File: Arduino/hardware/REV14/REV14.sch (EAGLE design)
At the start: 27 parts, among them IC2 ATMEGA168-AU, Q1 32768Hz, U1 RN2483, U2 TMP112, X1 SMA-142-0701-881/886, X2 SMA-142-0701-881/886

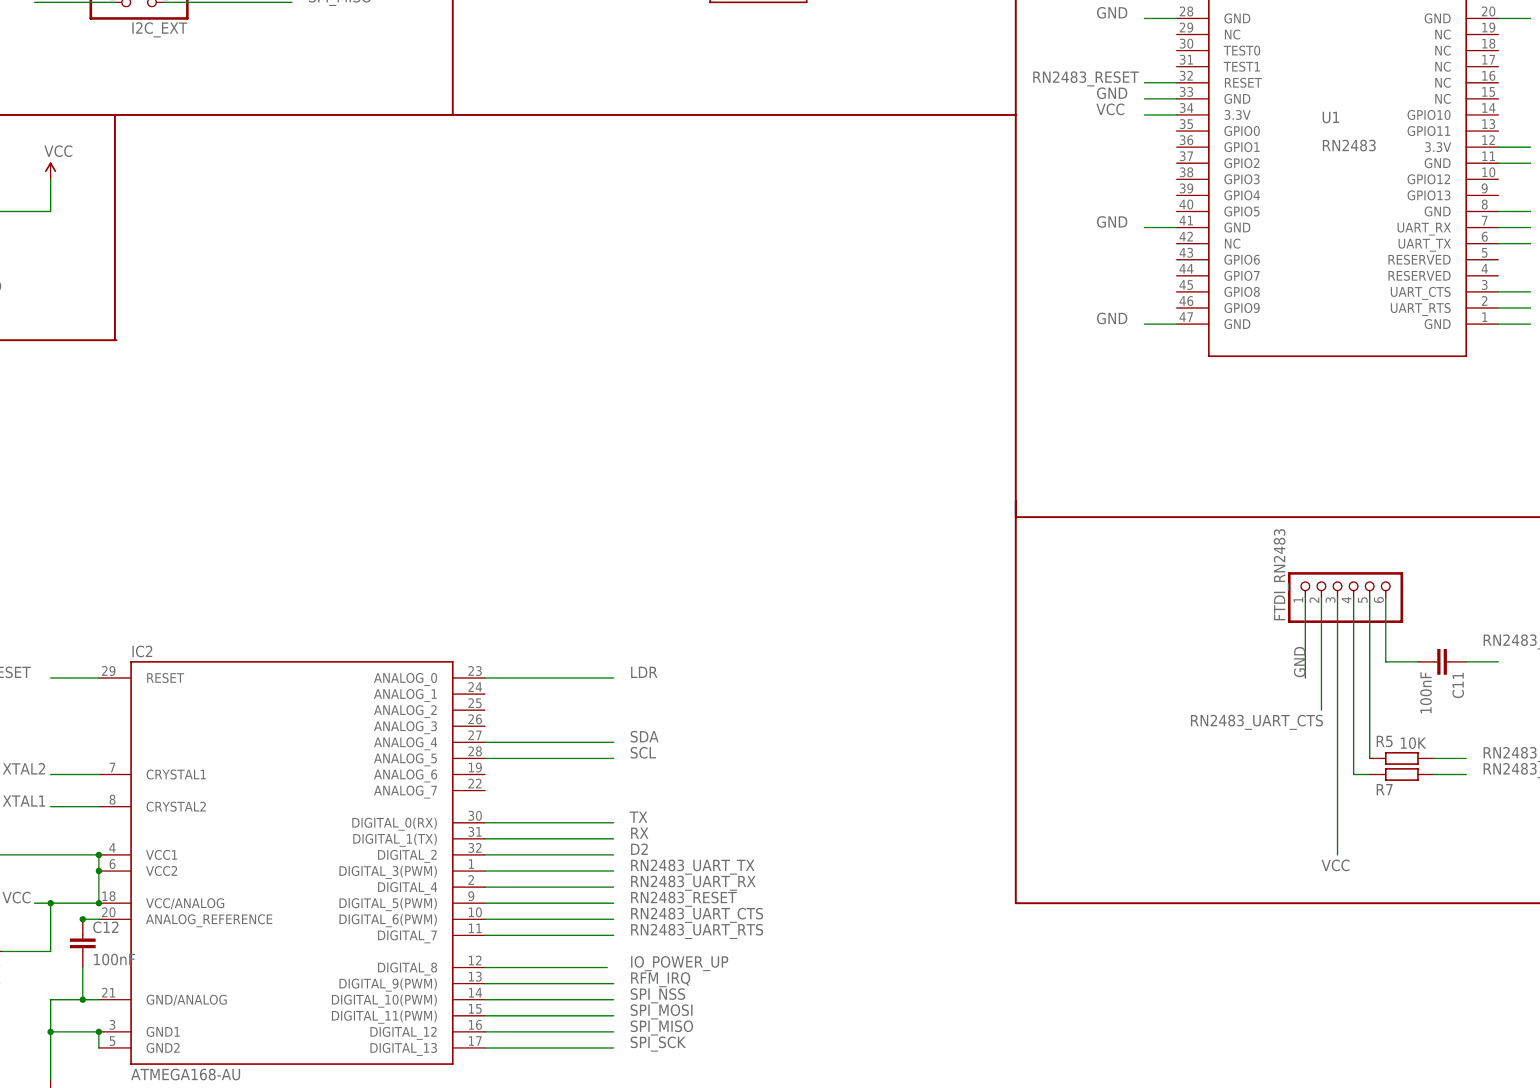
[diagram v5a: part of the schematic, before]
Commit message: charge pump added
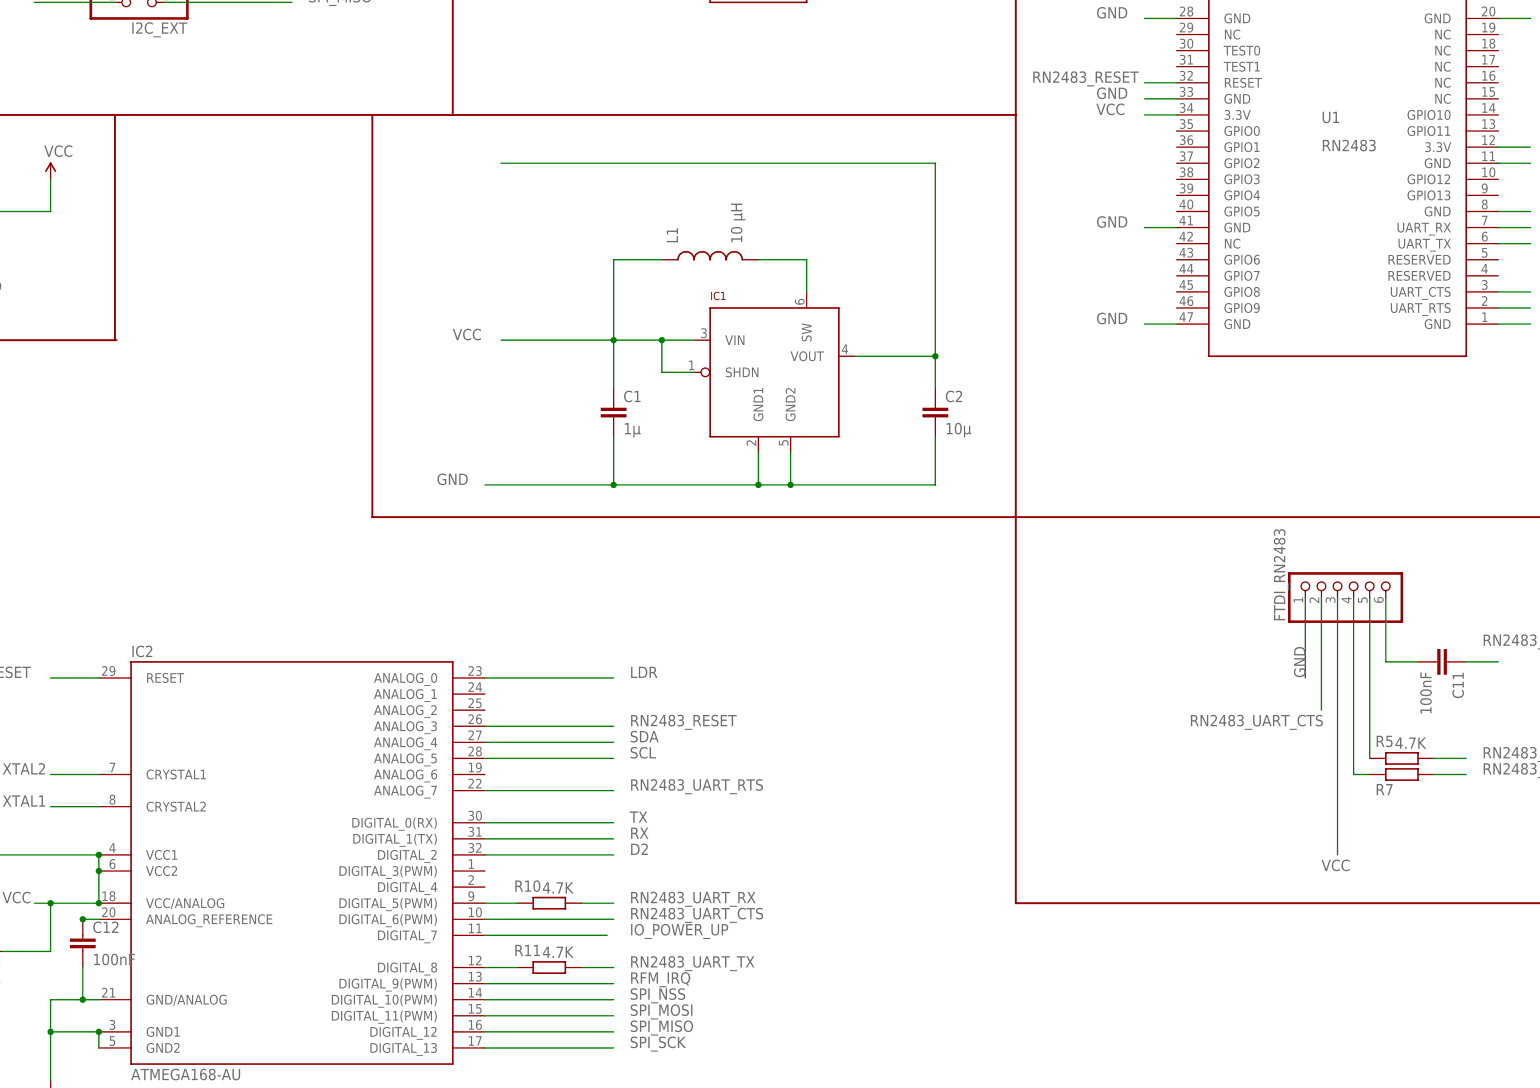
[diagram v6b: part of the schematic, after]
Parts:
- added C1: 1µ, SparkFun:CAP0603-CAP
- added C2: 10µ, SparkFun:CAP0805
- added IC1: LTC3525, JeeLabs:LTC3525
- added L1: 10 µH, SparkFun:INDUCTOR1210
- added R10, R11: 4.7K, resistor:R-EU_R0603
- R5, R7: value 10K -> 4.7K
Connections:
- new net N$10: IC1.SW, L1.2
- new net N$8: IC2.DIGITAL_5(PWM), R10.2
- new net N$9: IC2.DIGITAL_8, R11.2
- new net VCC1: C2.1, IC1.VOUT
- net GND: now also C1.2, C2.2, IC1.GND1, IC1.GND2
- net IO_POWER_UP: now also IC2.DIGITAL_7; no longer IC2.DIGITAL_8
- net RN2483_RESET: now also IC2.ANALOG_3; no longer IC2.DIGITAL_5(PWM)
- net RN2483_UART_RTS: now also IC2.ANALOG_7; no longer IC2.DIGITAL_7
- net RN2483_UART_RX: now also R10.1; no longer IC2.DIGITAL_4
- net RN2483_UART_TX: now also R11.1; no longer IC2.DIGITAL_3(PWM)
- net VCC: now also C1.1, IC1.SHDN, IC1.VIN, L1.1

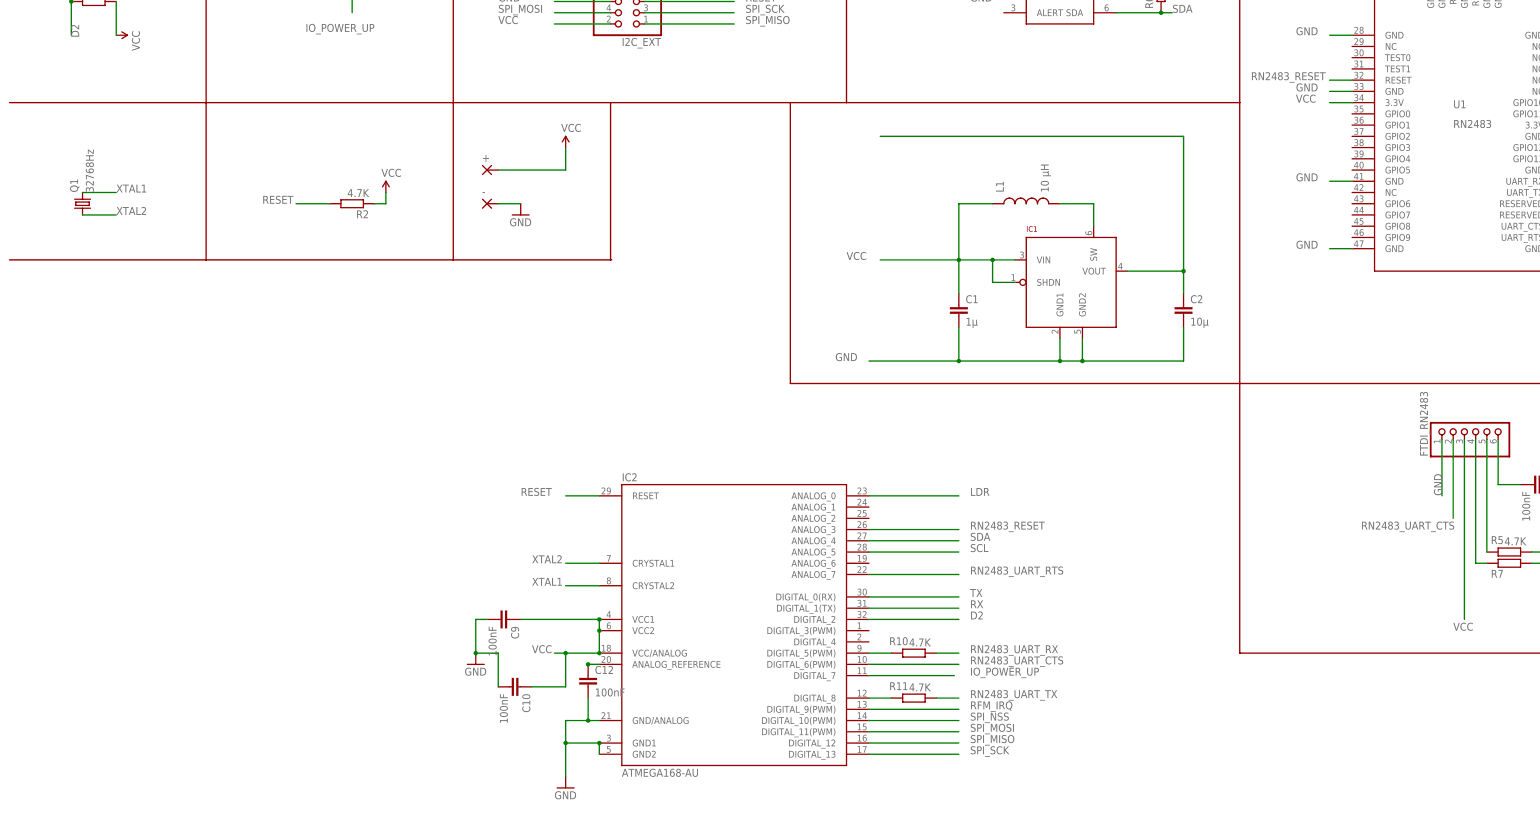
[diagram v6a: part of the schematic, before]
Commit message: routed with 1 wire left.
missing SHT21
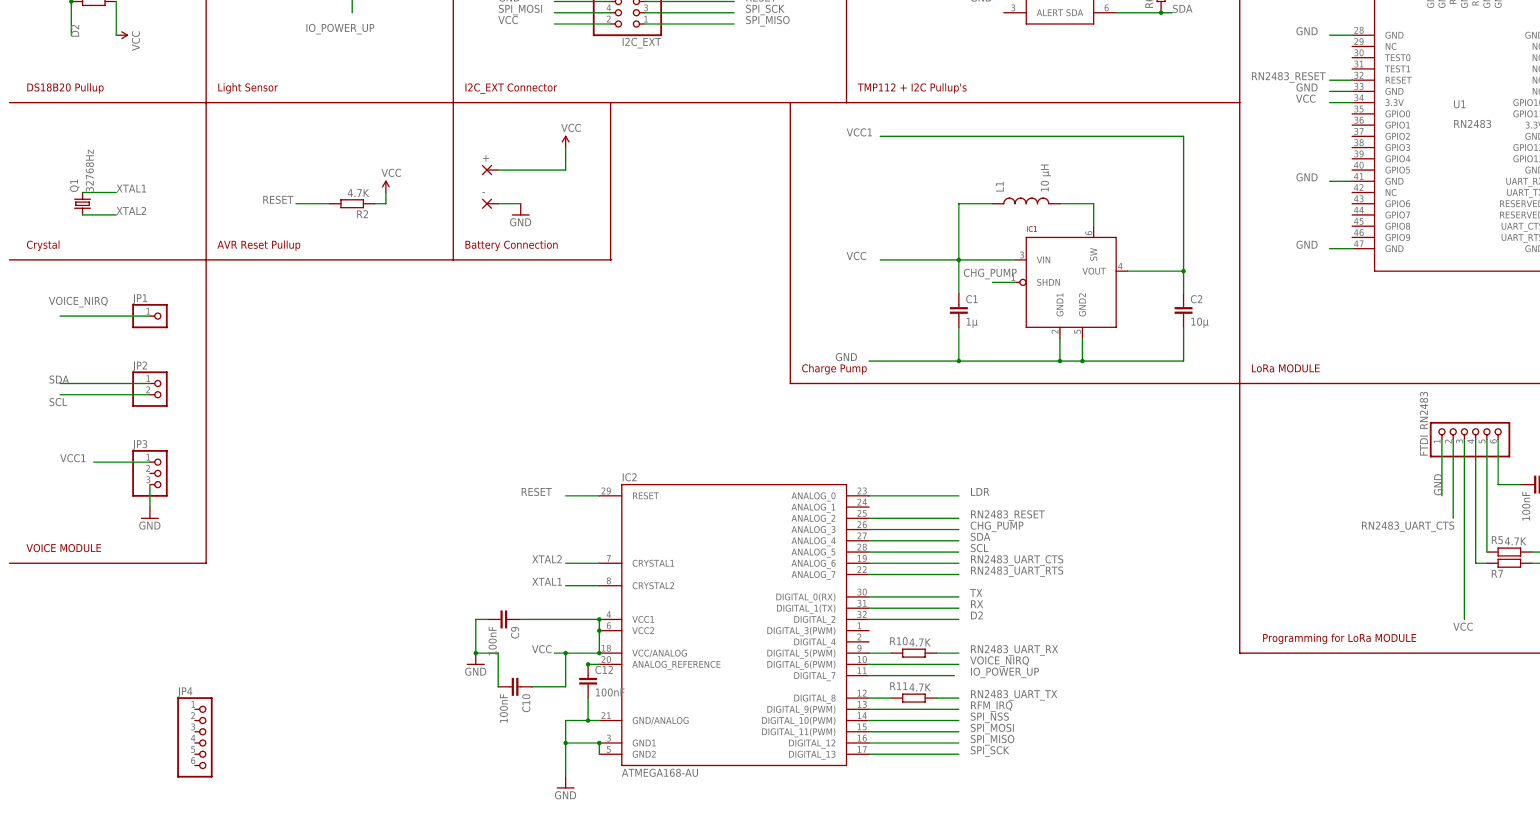
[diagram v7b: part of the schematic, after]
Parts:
- added JP1: (no value), pinhead:PINHD-1X1
- added JP2: (no value), pinhead:PINHD-1X2
- added JP3: (no value), pinhead:PINHD-1X3
- added JP4: (no value), pinhead:PINHD-1X6
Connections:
- new net CHG_PUMP: IC1.SHDN
- new net VOICE_NIRQ: IC2.DIGITAL_6(PWM), JP1.1
- net GND: now also JP3.3
- net RN2483_RESET: no longer IC2.ANALOG_3
- net RN2483_UART_CTS: no longer IC2.DIGITAL_6(PWM)
- net SCL: now also JP2.2
- net SDA: now also JP2.1
- net VCC: no longer IC1.SHDN
- net VCC1: now also JP3.1
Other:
- note added: "AVR Reset Pullup"
- note added: "Battery Connection"
- note added: "Charge Pump"
- note added: "Crystal"
- note added: "DS18B20 Pullup"
- note added: "I2C_EXT Connector"
- note added: "Light Sensor"
- note added: "LoRa MODULE"
- note added: "Programming for LoRa MODULE"
- note added: "TMP112 + I2C Pullup's"
- note added: "VOICE MODULE"
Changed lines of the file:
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@@
 <part name="IC1" library="JeeLabs" deviceset="LTC3525" device=""/>
 <part name="L1" library="SparkFun" deviceset="INDUCTOR" device="1210" value="10 µH"/>
+<part name="JP1" library="pinhead" deviceset="PINHD-1X1" device=""/>
+<part name="JP2" library="pinhead" deviceset="PINHD-1X2" device=""/>
+<part name="JP3" library="pinhead" deviceset="PINHD-1X3" device=""/>
+<part name="GND8" library="SparkFun-Aesthetics" deviceset="GND" device=""/>
+<part name="JP4" library="pinhead" deviceset="PINHD-1X6" device=""/>
 </parts>
 <sheets>
@@
 <wire x1="180.34" y1="129.54" x2="180.34" y2="193.04" width="0.3048" layer="94"/>
 <wire x1="180.34" y1="129.54" x2="281.94" y2="129.54" width="0.3048" layer="94"/>
+<wire x1="48.26" y1="88.9" x2="48.26" y2="157.48" width="0.3048" layer="94"/>
+<wire x1="3.81" y1="88.9" x2="48.26" y2="88.9" width="0.3048" layer="94"/>
+<text x="7.62" y="91.44" size="1.778" layer="94">VOICE MODULE</text>
+<text x="7.62" y="160.02" size="1.778" layer="94">Crystal</text>
+<text x="50.8" y="160.02" size="1.778" layer="94">AVR Reset Pullup</text>
+<text x="106.68" y="160.02" size="1.778" layer="94">Battery Connection</text>
+<text x="7.62" y="195.58" size="1.778" layer="94">DS18B20 Pullup</text>
+<text x="50.8" y="195.58" size="1.778" layer="94">Light Sensor </text>
+<text x="106.68" y="195.58" size="1.778" layer="94">I2C_EXT Connector</text>
+<text x="195.58" y="195.58" size="1.778" layer="94">TMP112 + I2C Pullup's</text>
+<text x="182.88" y="132.08" size="1.778" layer="94">Charge Pump</text>
+<text x="284.48" y="132.08" size="1.778" layer="94">LoRa MODULE</text>
+<text x="287.02" y="71.12" size="1.778" layer="94">Programming for LoRa MODULE</text>
 </plain>
 <instances>
@@
 <instance part="IC1" gate="G$1" x="243.84" y="152.4"/>
 <instance part="L1" gate="G$1" x="233.68" y="170.18" rot="R90"/>
+<instance part="JP1" gate="G$1" x="38.1" y="144.78"/>
+<instance part="JP2" gate="G$1" x="38.1" y="127"/>
+<instance part="JP3" gate="A" x="38.1" y="109.22"/>
+<instance part="GND8" gate="1" x="35.56" y="99.06"/>
+<instance part="JP4" gate="A" x="48.26" y="48.26"/>
 </instances>
 <busses>
@@
 <pinref part="IC1" gate="G$1" pin="GND2"/>
 <label x="190.5" y="134.62" size="1.778" layer="95"/>
+</segment>
+<segment>
+<pinref part="JP3" gate="A" pin="3"/>
+<pinref part="GND8" gate="1" pin="GND"/>
+<wire x1="35.56" y1="101.6" x2="35.56" y2="106.68" width="0.1524" layer="91"/>
 </segment>
 </net>
@@
 </segment>
 <segment>
-<wire x1="231.14" y1="157.48" x2="226.06" y2="157.48" width="0.1524" layer="91"/>
-<wire x1="226.06" y1="157.48" x2="218.44" y2="157.48" width="0.1524" layer="91"/>
+<wire x1="231.14" y1="157.48" x2="218.44" y2="157.48" width="0.1524" layer="91"/>
 <wire x1="218.44" y1="157.48" x2="200.66" y2="157.48" width="0.1524" layer="91"/>
 <wire x1="218.44" y1="149.86" x2="218.44" y2="157.48" width="0.1524" layer="91"/>
-<wire x1="231.14" y1="152.4" x2="226.06" y2="152.4" width="0.1524" layer="91"/>
-<wire x1="226.06" y1="152.4" x2="226.06" y2="157.48" width="0.1524" layer="91"/>
 <wire x1="226.06" y1="170.18" x2="218.44" y2="170.18" width="0.1524" layer="91"/>
 <wire x1="218.44" y1="170.18" x2="218.44" y2="157.48" width="0.1524" layer="91"/>
 <junction x="218.44" y="157.48"/>
-<junction x="226.06" y="157.48"/>
 <pinref part="IC1" gate="G$1" pin="VIN"/>
 <pinref part="C1" gate="G$1" pin="1"/>
-<pinref part="IC1" gate="G$1" pin="SHDN"/>
 <pinref part="L1" gate="G$1" pin="1"/>
 <label x="193.04" y="157.48" size="1.778" layer="95"/>
@@
 <pinref part="I2C_EXT" gate="A" pin="11"/>
 </segment>
+<segment>
+<wire x1="15.24" y1="129.54" x2="35.56" y2="129.54" width="0.1524" layer="91"/>
+<label x="12.7" y="129.54" size="1.778" layer="95"/>
+<pinref part="JP2" gate="G$1" pin="1"/>
+</segment>
 </net>
 <net name="SCL" class="0">
@@
 <pinref part="I2C_EXT" gate="A" pin="9"/>
 </segment>
+<segment>
+<wire x1="35.56" y1="127" x2="15.24" y2="127" width="0.1524" layer="91"/>
+<label x="12.7" y="124.46" size="1.778" layer="95"/>
+<pinref part="JP2" gate="G$1" pin="2"/>
+</segment>
 </net>
 <net name="RESET" class="0">
@@
 </segment>
 <segment>
-<wire x1="198.12" y1="96.52" x2="218.44" y2="96.52" width="0.1524" layer="91"/>
-<label x="220.98" y="96.52" size="1.778" layer="95"/>
-<pinref part="IC2" gate="1" pin="ANALOG_3"/>
+<wire x1="198.12" y1="99.06" x2="218.44" y2="99.06" width="0.1524" layer="91"/>
+<label x="220.98" y="99.06" size="1.778" layer="95"/>
 </segment>
 </net>
@@
 <net name="RN2483_UART_CTS" class="0">
 <segment>
-<pinref part="IC2" gate="1" pin="DIGITAL_6(PWM)"/>
-<wire x1="198.12" y1="66.04" x2="218.44" y2="66.04" width="0.1524" layer="91"/>
-<label x="220.98" y="66.04" size="1.778" layer="95"/>
-</segment>
-<segment>
 <wire x1="358.14" y1="165.1" x2="363.22" y2="165.1" width="0.1524" layer="91"/>
 <label x="365.76" y="165.1" size="1.778" layer="95"/>
@@
 <label x="309.372" y="96.52" size="1.778" layer="95"/>
 <pinref part="FTDI_RN2483" gate="A" pin="2"/>
+</segment>
+<segment>
+<wire x1="198.12" y1="88.9" x2="218.44" y2="88.9" width="0.1524" layer="91"/>
+<label x="220.98" y="88.9" size="1.778" layer="95"/>
 </segment>
 </net>
@@
 <pinref part="C2" gate="G$1" pin="1"/>
 <pinref part="IC1" gate="G$1" pin="VOUT"/>
+<label x="193.04" y="185.42" size="1.778" layer="95"/>
+</segment>
+<segment>
+<wire x1="22.86" y1="111.76" x2="35.56" y2="111.76" width="0.1524" layer="91"/>
+<label x="15.24" y="111.76" size="1.778" layer="95"/>
+<pinref part="JP3" gate="A" pin="1"/>
 </segment>
 </net>
@@
 </segment>
 </net>
+<net name="CHG_PUMP" class="1">
+<segment>
+<pinref part="IC1" gate="G$1" pin="SHDN"/>
+<wire x1="231.14" y1="152.4" x2="226.06" y2="152.4" width="0.1524" layer="91"/>
+<label x="219.456" y="153.67" size="1.778" layer="95"/>
+</segment>
+<segment>
+<wire x1="218.44" y1="96.52" x2="198.12" y2="96.52" width="0.1524" layer="91"/>
+<label x="220.98" y="96.52" size="1.778" layer="95"/>
+</segment>
+</net>
+<net name="VOICE_NIRQ" class="0">
+<segment>
+<pinref part="IC2" gate="1" pin="DIGITAL_6(PWM)"/>
+<wire x1="198.12" y1="66.04" x2="218.44" y2="66.04" width="0.1524" layer="91"/>
+<label x="220.98" y="66.04" size="1.778" layer="95"/>
+</segment>
+<segment>
+<wire x1="15.24" y1="144.78" x2="35.56" y2="144.78" width="0.1524" layer="91"/>
+<label x="12.7" y="147.32" size="1.778" layer="95"/>
+<pinref part="JP1" gate="G$1" pin="1"/>
+</segment>
+</net>
